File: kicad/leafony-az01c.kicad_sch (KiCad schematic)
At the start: 22 parts, among them CN1 Leafony Bus, J1 CX90M-16P, U1 TS3A4751RUCR, U2 USBLC6-2P6, U3 FT234XD, U4 TPS6282533DMQR

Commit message: ディレクトリを整理
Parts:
- CN1: now left out of the parts list
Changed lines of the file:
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@@
 		(unit 1)
 		(exclude_from_sim no)
-		(in_bom yes)
+		(in_bom no)
 		(on_board yes)
 		(dnp no)

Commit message: BOM修正
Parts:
- U1: value TS3A4751RUCR -> TS3A4741DCNR; MPN TS3A4751RUCR -> TS3A4741DCNR
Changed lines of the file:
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@@
 			)
 		)
-		(property "Value" "TS3A4751RUCR"
+		(property "Value" "TS3A4741DCNR"
 			(at 180.34 78.74 0)
 			(effects
@@
 			)
 		)
-		(property "MPN" "TS3A4751RUCR"
+		(property "MPN" "TS3A4741DCNR"
 			(at 149.86 83.82 0)
 			(effects

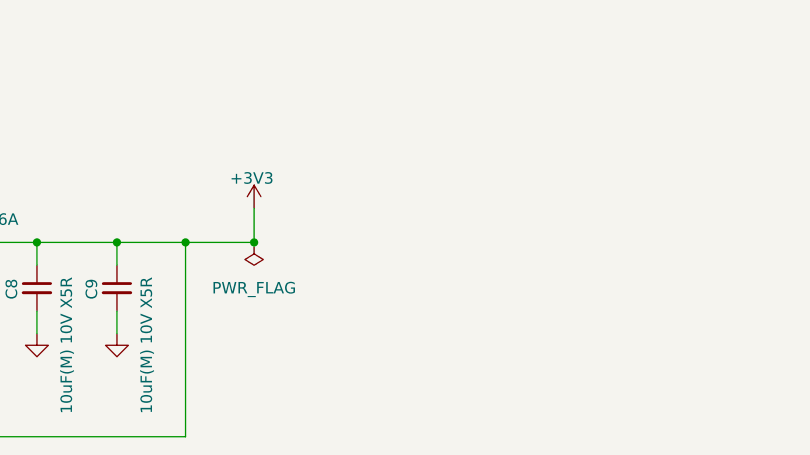
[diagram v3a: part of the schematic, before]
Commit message: BOMとガーバーを更新
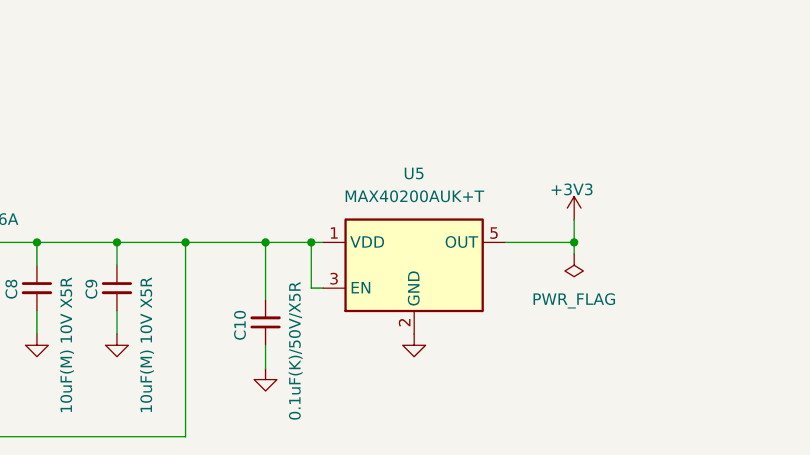
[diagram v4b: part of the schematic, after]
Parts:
- added C10: 0.1uF(K)/50V/X5R, Capacitor_SMD:C_0402_1005Metric, symbol Device:C_Small
- added U5: MAX40200AUK+T, Package_TO_SOT_SMD:SOT-23-5, symbol Analog_Switch:MAX40200AUK
- L1: MPN DFE201610E-R47M -> DFE201610E-R47M=P2
- U3: MPN FT234XD -> FT234XD-T
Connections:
- net +3V3: now also U5.5 (OUT); no longer C8.1, C9.1, L1.2, U4.3 (FB)
- net GND: now also C10.1, U5.2 (GND)
- new net: C10.2, C8.1, C9.1, L1.2, U4.3 (FB), U5.1 (VDD), U5.3 (EN)
